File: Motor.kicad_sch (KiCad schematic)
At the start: 41 parts, among them U1 MCF8315C1VQRGFRQ1

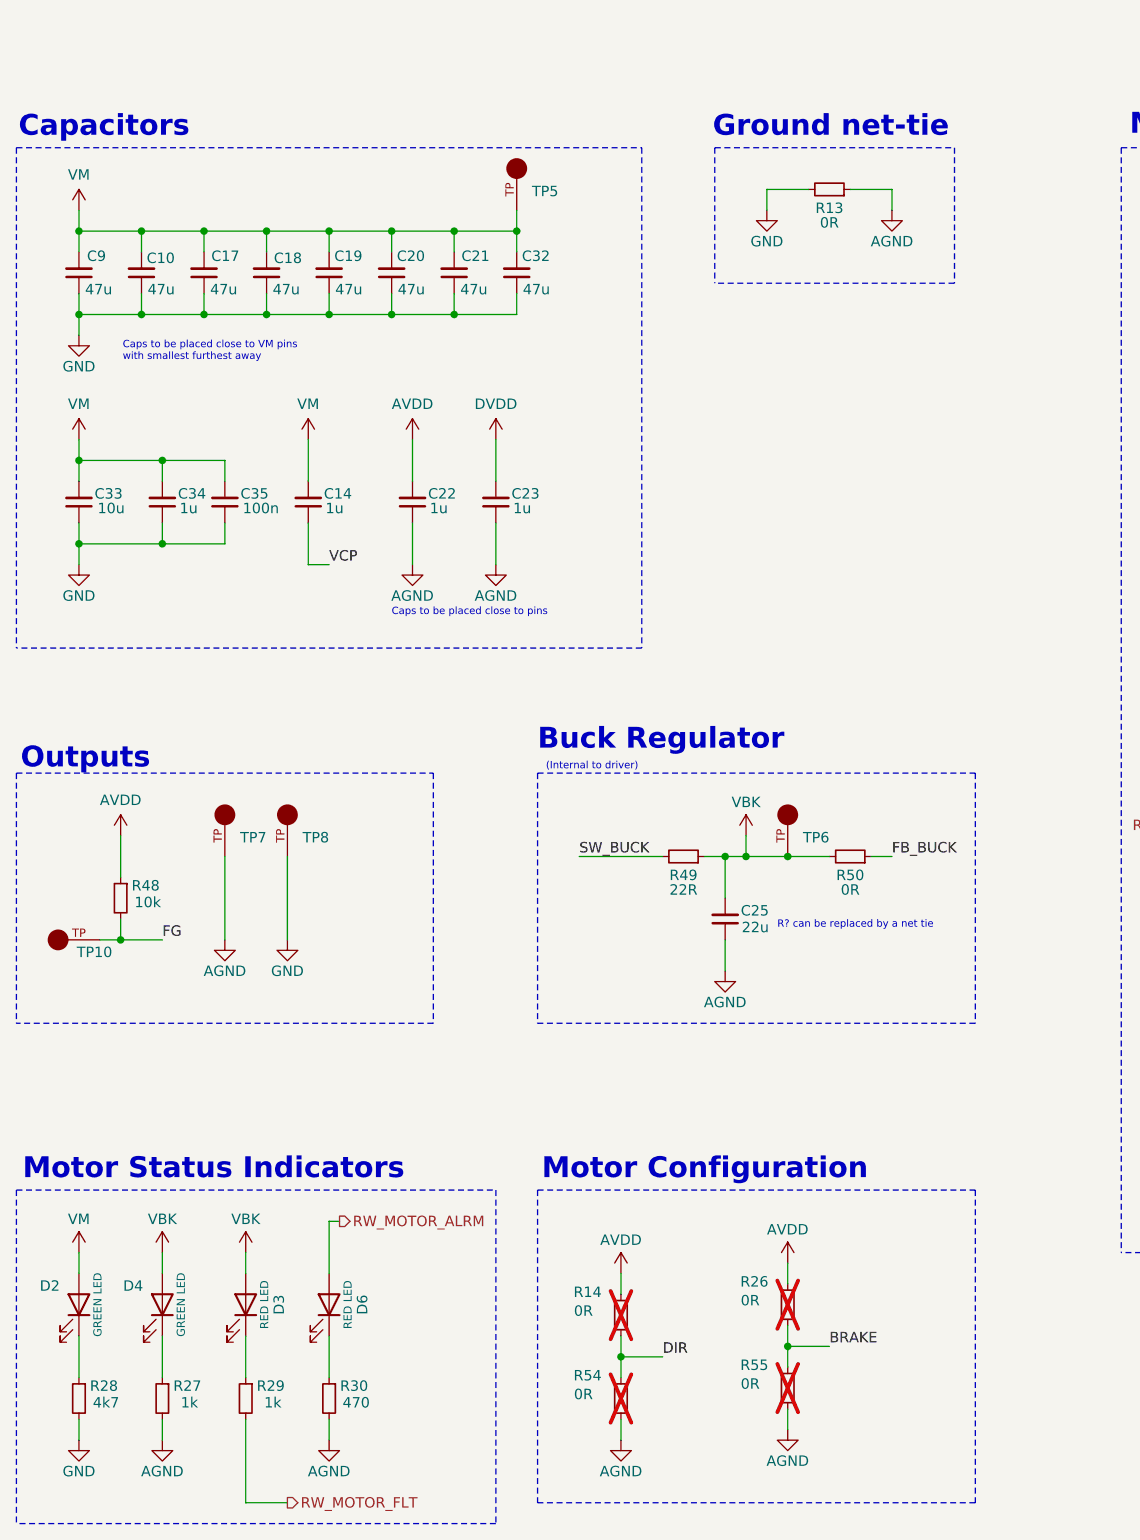
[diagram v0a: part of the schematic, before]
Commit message: Push requested changes - silkscreen, copper width, pi filter
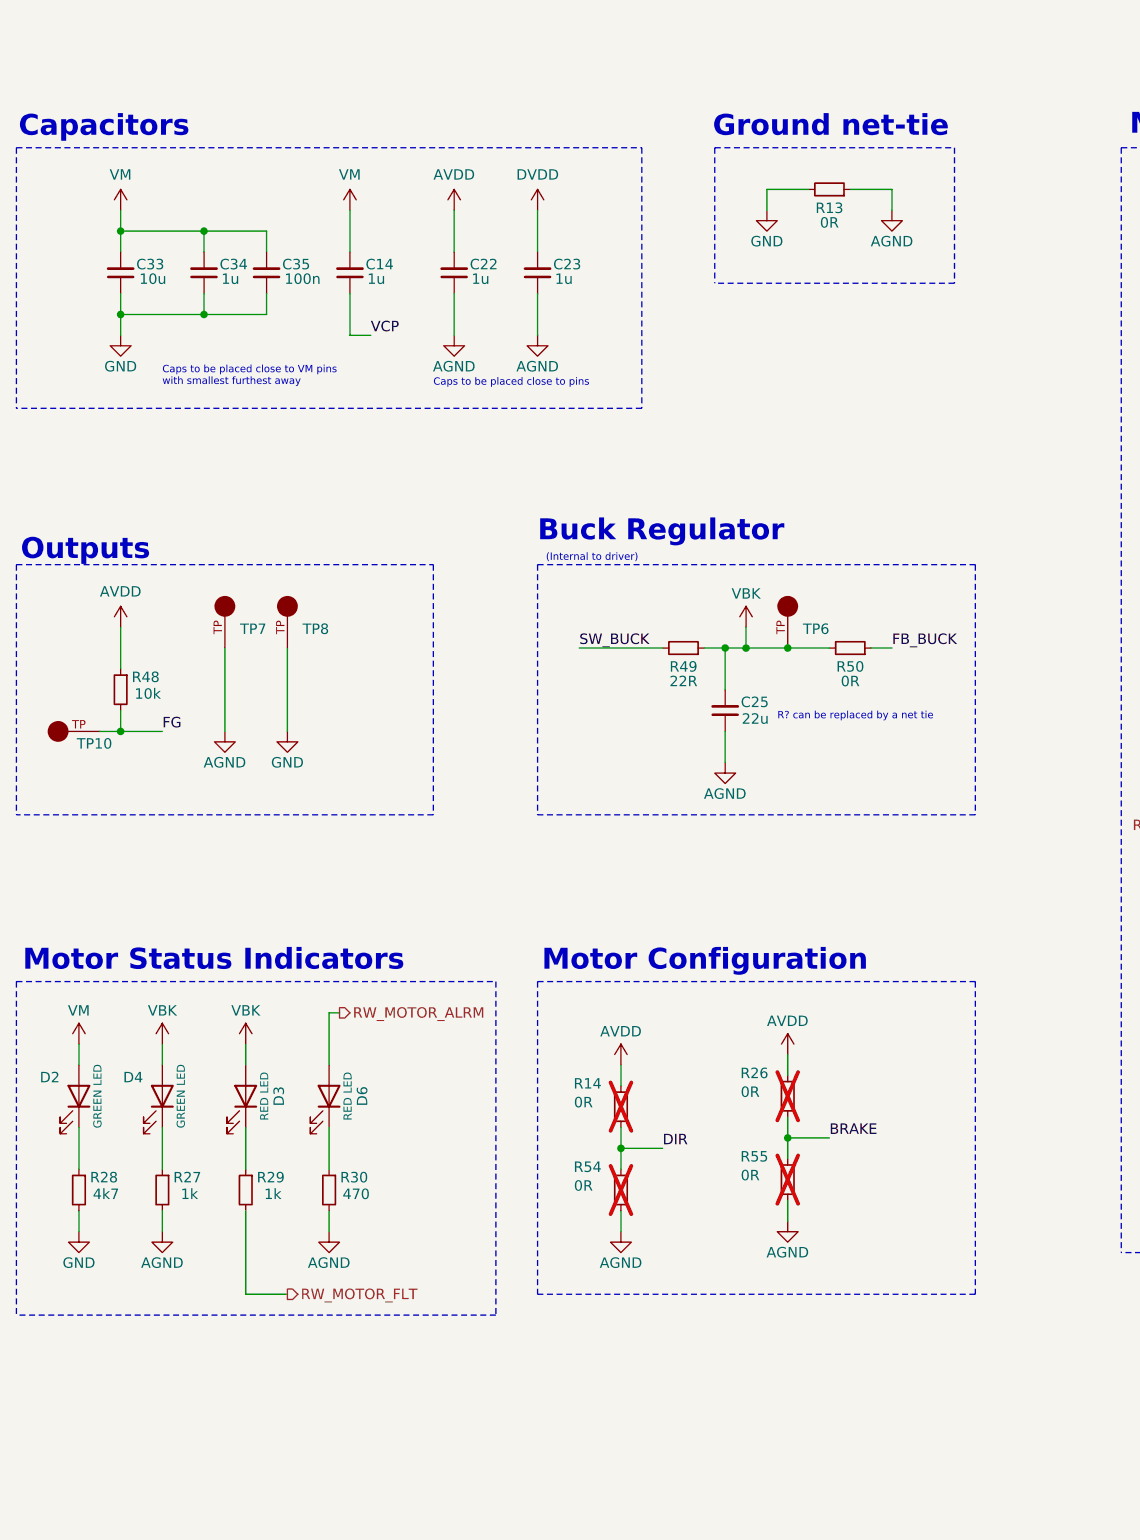
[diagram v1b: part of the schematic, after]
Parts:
- removed C10, C17, C18, C19, C20, C21, C32, C9: 47u, Capacitor_SMD:C_1206_3216Metric_Pad1.33x1.80mm_HandSolder, symbol Device:C_Small
- removed TP5: ~, Argus_RW_Library:KEYSTONE_5001, symbol Argus_RW_Library:5001
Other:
- moved on the sheet: C14, C22, C23, C25, C33, C34, C35, D2, D3, D4, D6, R14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

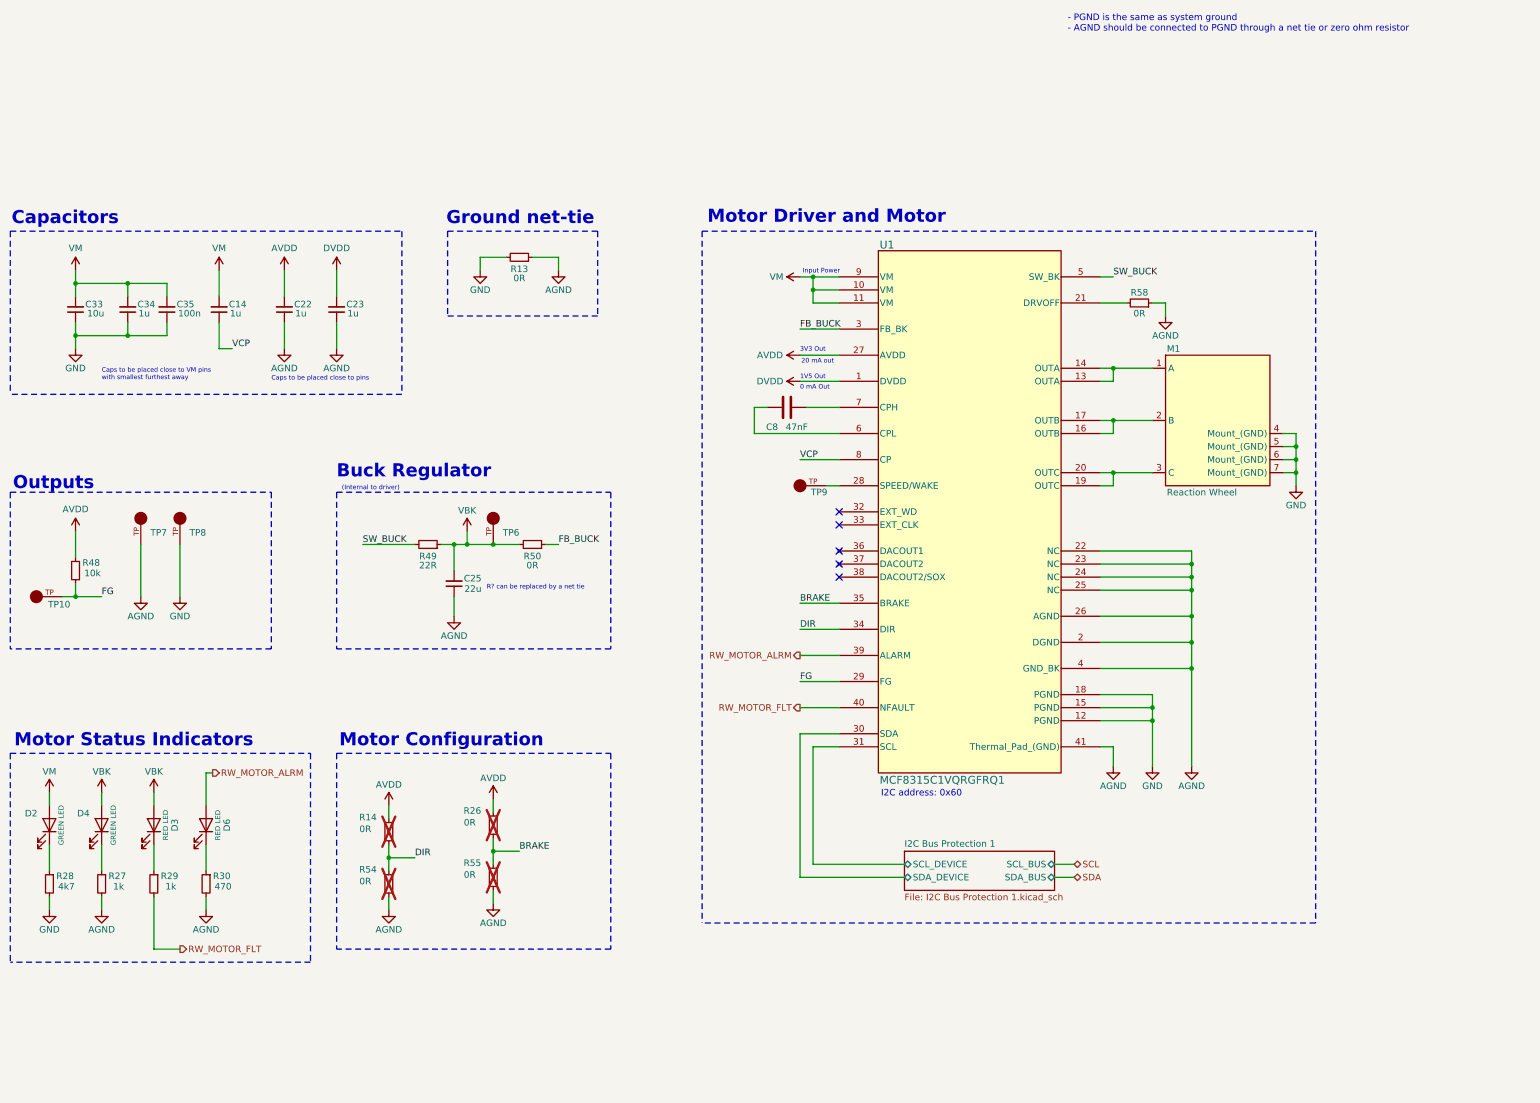
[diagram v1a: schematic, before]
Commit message: Add and correct BOM for easy Digikey ordering
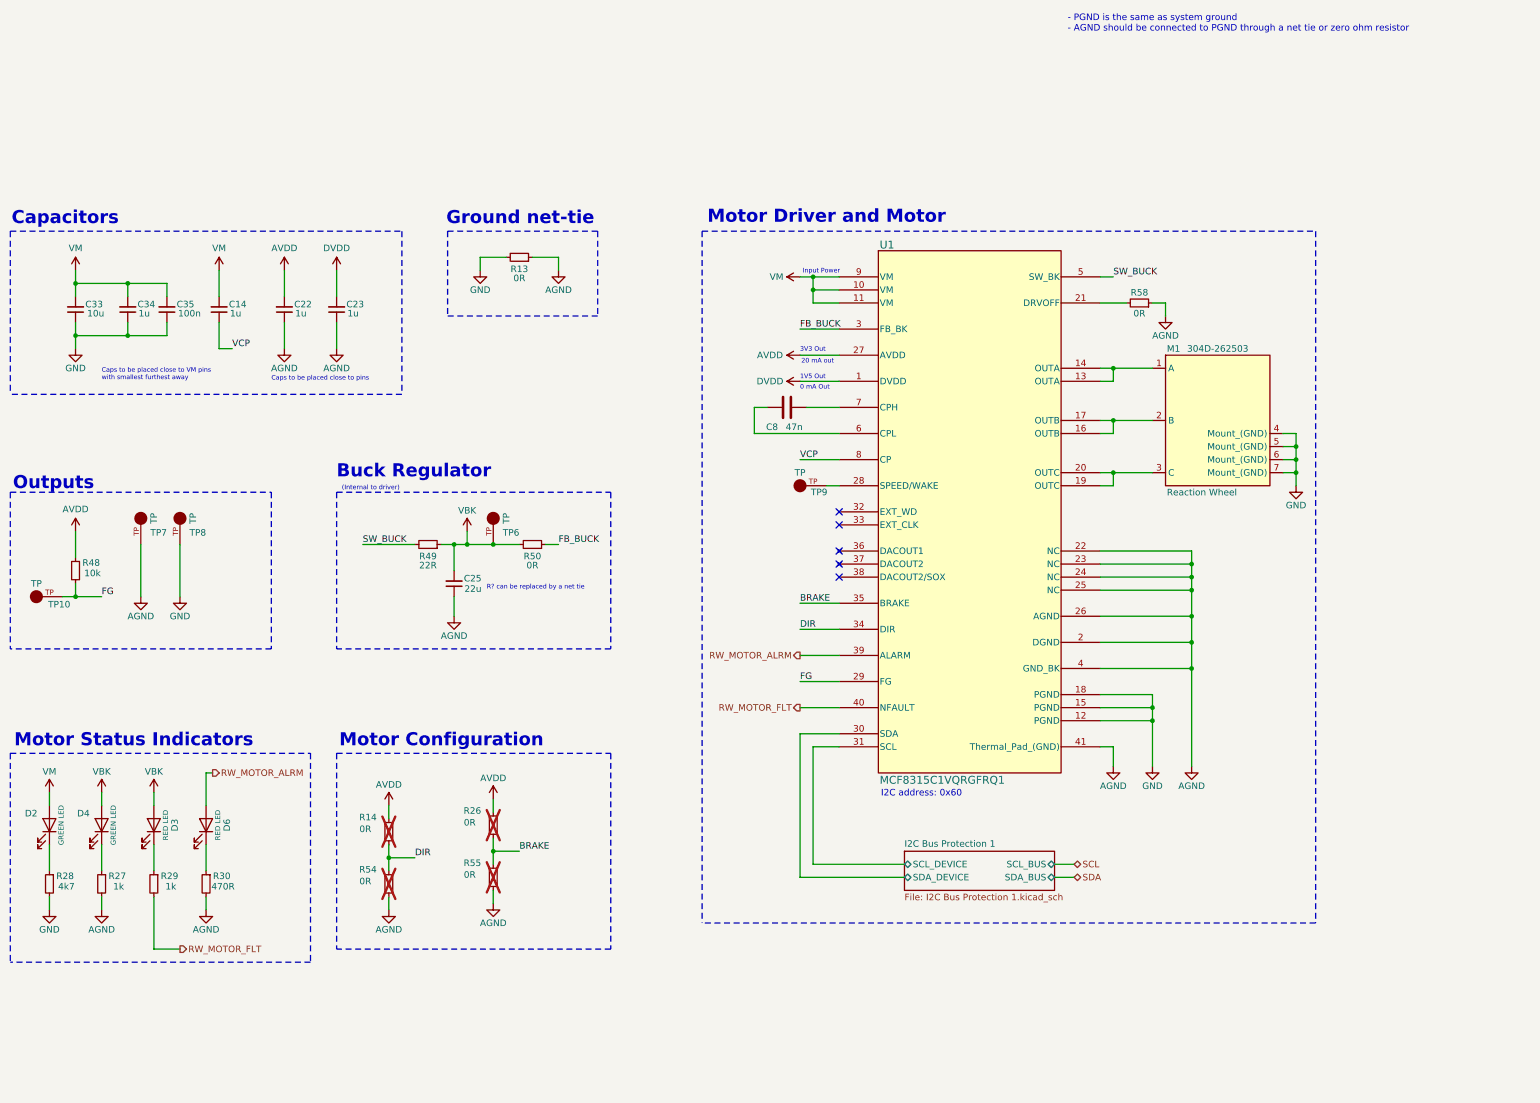
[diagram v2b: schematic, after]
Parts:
- C14, C22, C23, C34: Digikey PN (none) -> 1276-1184-1-ND; MPN (none) -> CL10B105KA8NNNC
- C25: Digikey (none) -> https://www.digikey.com/en/products/detail/samsung-electro-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; Digikey PN (none) -> 1276-1274-1-ND; MPN (none) -> CL10A226MP8NUNE; Part (none) -> CL10A226MP8NUNE
- C33: Digikey PN (none) -> 1276-1804-1-ND; MPN (none) -> CL31B106KAHNNNE
- C35: Digikey PN (none) -> 399-C0402C103K3RACTUCT-ND; MPN (none) -> C0402C103K3RACTU
- C8: value 47nF -> 47n; Digikey PN (none) -> 490-4934-1-ND; MPN (none) -> GCM188R71H473KA55D
- D2, D4: Digikey (none) -> https://www.digikey.com/en/products/detail/inolux/IN-S63AT5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; Digikey PN (none) -> 1830-1064-1-ND; MPN (none) -> IN-S63AT5A; Part (none) -> IN-S63AT5A
- D3, D6: Digikey (none) -> https://www.digikey.com/en/products/detail/inolux/IN-S63ATR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; Digikey PN (none) -> 1830-1065-1-ND; MPN (none) -> IN-S63ATR; Part (none) -> IN-S63ATR
- M1: value ~ -> 304D-262503; Digikey (none) -> https://www.digikey.com/en/products/detail/attend-technolog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; Digikey PN (none) -> 4827-304D-262503CT-ND; MPN (none) -> 304D-262503; Part (none) -> 304D-262503
- R13, R50: Digikey (none) -> https://www.digikey.com/en/products/detail/yageo/RC0805JR-0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; Digikey PN (none) -> 311-0.0ARCT-ND; MPN (none) -> RC0805JR-070RL; Part (none) -> RC0805JR-070RL
- R14, R26, R54, R55, R58: Digikey (none) -> https://www.digikey.com/en/products/detail/yageo/RC0402JR-0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; Digikey PN (none) -> 311-0.0JRCT-ND; MPN (none) -> RC0402JR-070RL; Part (none) -> RC0402JR-070RL
- R27, R29: Digikey (none) -> https://www.digikey.com/en/products/detail/yageo/RC0603FR-0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; Digikey PN (none) -> 311-1.00KHRCT-ND; MPN (none) -> RC0603FR-071KL; Part (none) -> RC0603FR-071KL
- R28: Digikey (none) -> https://www.digikey.com/en/products/detail/yageo/RC0603FR-0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; Digikey PN (none) -> 311-4.70KHRCT-ND; MPN (none) -> RC0603FR-074K7L; Part (none) -> RC0603FR-074K7L
- R30: value 470 -> 470R; Digikey (none) -> https://www.digikey.com/en/products/detail/yageo/RC0603FR-1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; Digikey PN (none) -> 13-RC0603FR-13470RLCT-ND; MPN (none) -> RC0603FR-13470RL; Part (none) -> RC0603FR-13470RL
- R48: Digikey (none) -> https://www.digikey.com/en/products/detail/yageo/RC0603FR-0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; Digikey PN (none) -> 311-10.0KHRCT-ND; MPN (none) -> RC0603FR-0710KL; Part (none) -> RC0603FR-0710KL
- R49: Digikey PN (none) -> 541-CRCW251222R0FKEGHPCT-ND; MPN (none) -> CRCW251222R0FKEGHP
- TP10, TP6, TP7, TP8, TP9: value ~ -> TP; Digikey (none) -> https://www.digikey.com/en/products/detail/keystone-electro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; Digikey PN (none) -> 36-5001-ND; MPN (none) -> 5001; Part (none) -> 5001
- U1: Digikey (none) -> https://www.digikey.com/en/products/detail/texas-instrument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; Digikey PN (none) -> 296-MCF8315C1VQRGFRQ1CT-ND; MPN (none) -> MCF8315C1VQRGFRQ1; Part (none) -> MCF8315C1VQRGFRQ1
